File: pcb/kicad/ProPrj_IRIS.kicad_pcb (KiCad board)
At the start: 4 copper layers, 92.7 x 72.5 mm, 259 parts

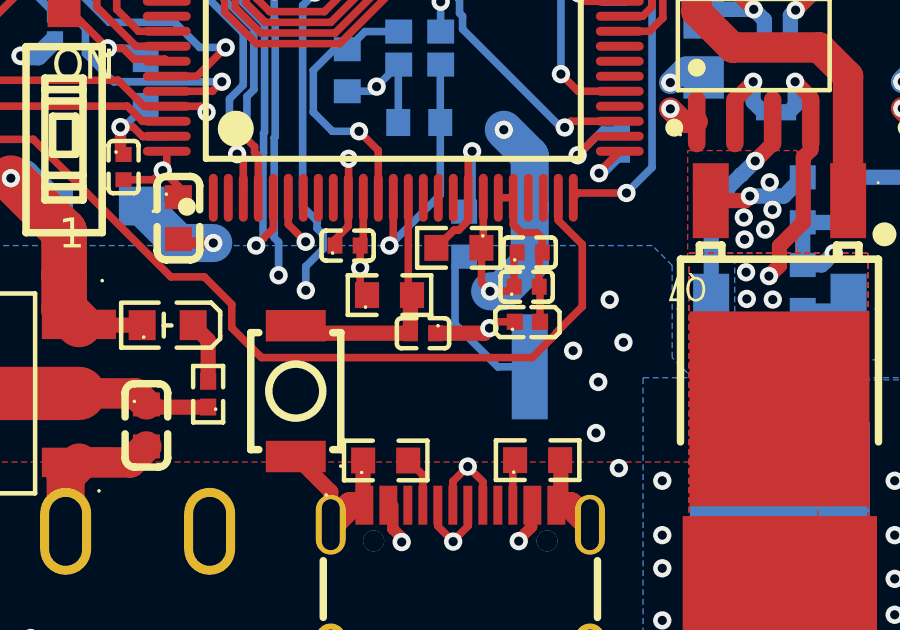
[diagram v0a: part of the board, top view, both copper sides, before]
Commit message: corrected nrst decoupling capacitor - thanks to @kaipereira for the tip
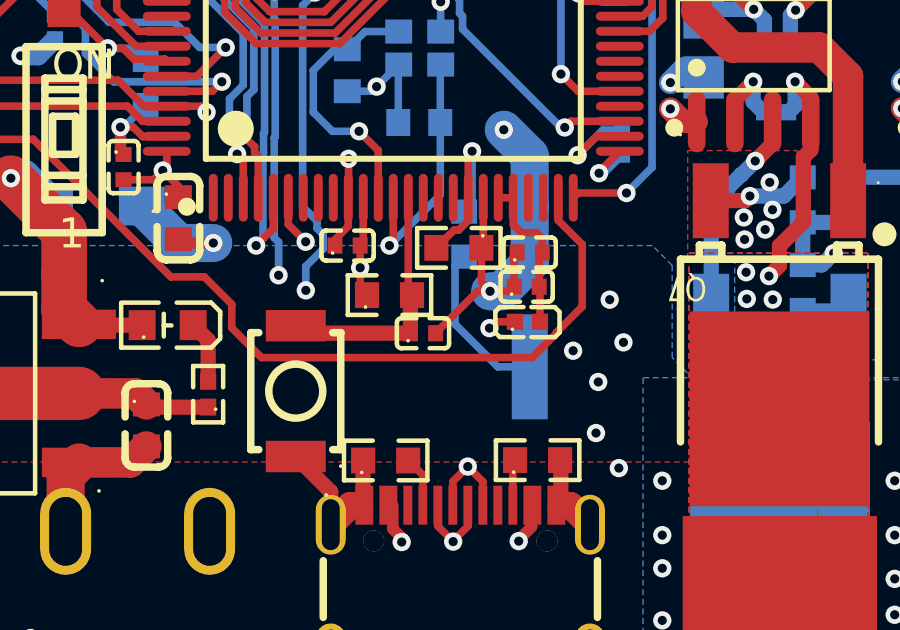
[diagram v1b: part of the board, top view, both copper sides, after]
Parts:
- turned C121 to 0 degrees
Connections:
- C121 pad 1: 3V3 -> $1N96765
- C121 pad 2: $1N96765 -> GND
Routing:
- net GND: track 332.8 -> 335.2 mm
- net 3V3: track 221.8 -> 219.9 mm
